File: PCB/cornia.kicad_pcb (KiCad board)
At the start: 2 copper layers, 159.3 x 104.6 mm, 76 parts, among them J1 Conn_01x01_Pin, SW1 SW_Push, SW10 SW_Push, SW11 SW_Push, SW12 SW_Push, SW13 SW_Push, SW14 SW_Push, SW15 SW_Push, SW16 SW_Push, SW17 SW_Push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

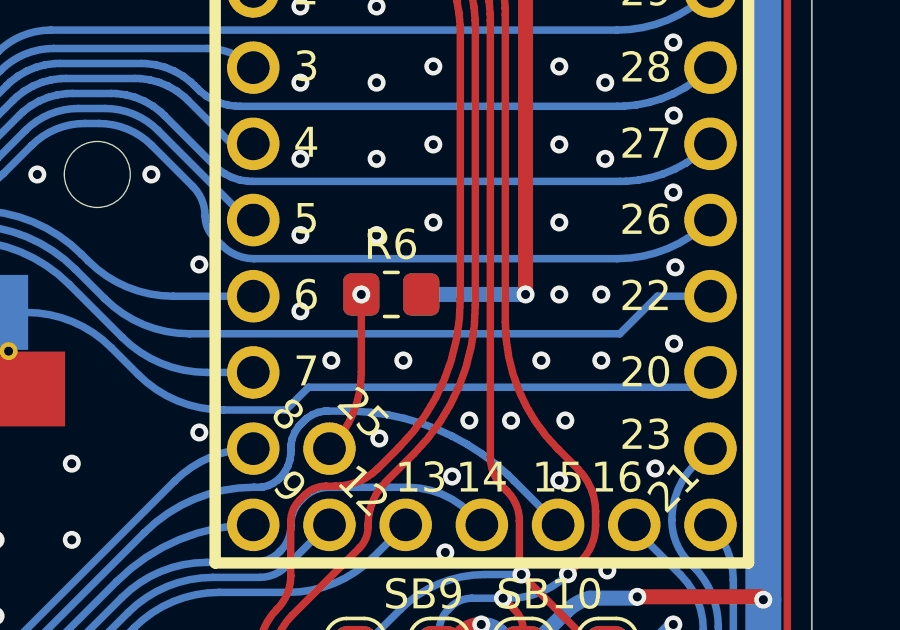
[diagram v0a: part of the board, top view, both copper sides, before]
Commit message: [PCB/Output] Add teardrop + update output
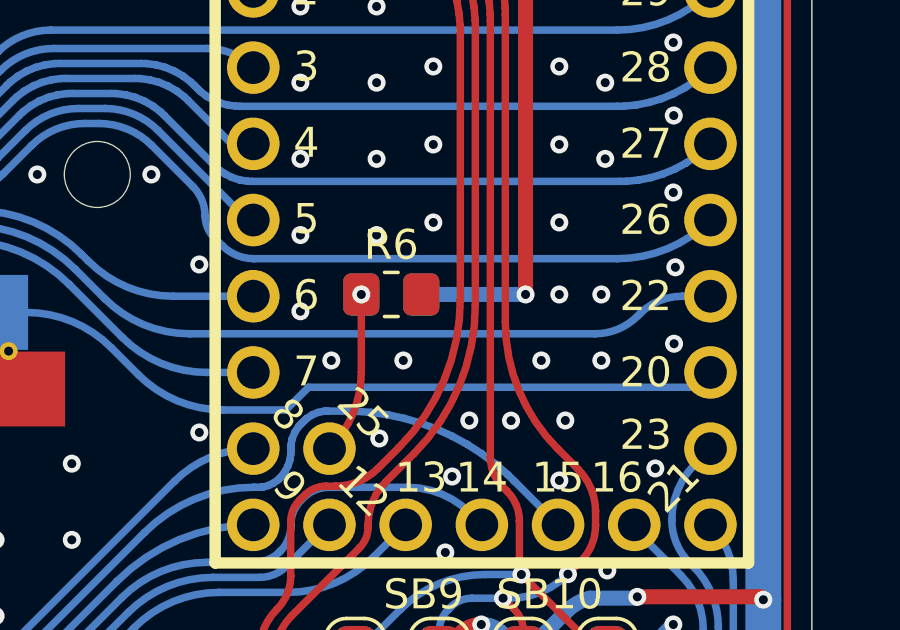
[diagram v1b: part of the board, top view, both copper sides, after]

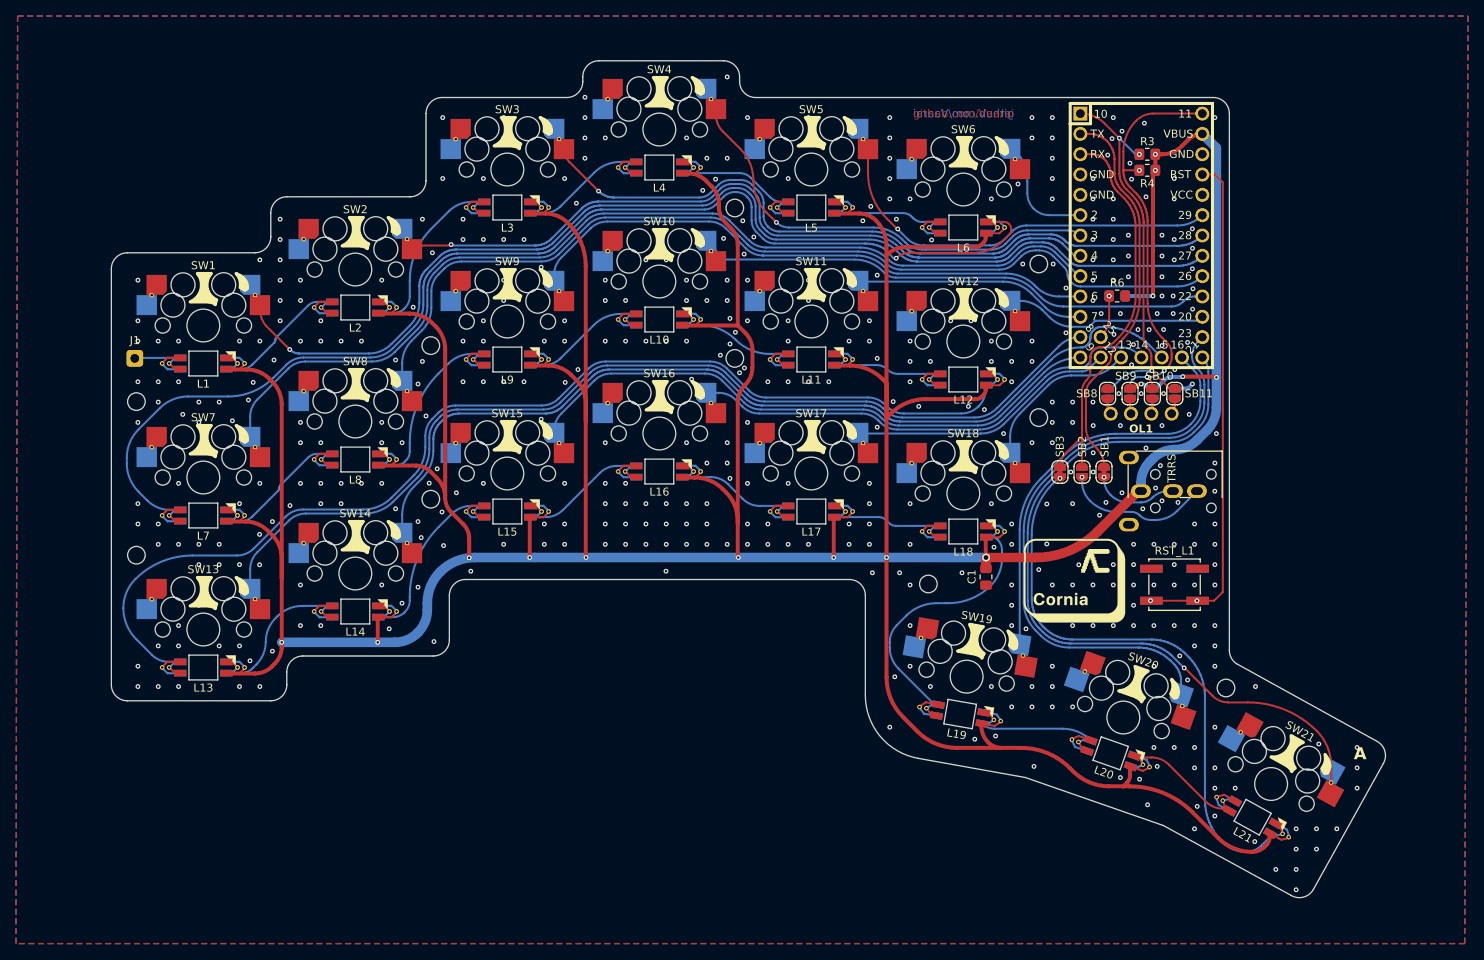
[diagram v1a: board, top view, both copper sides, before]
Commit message: [PCB] Fix RGB Led pin assignment mistake
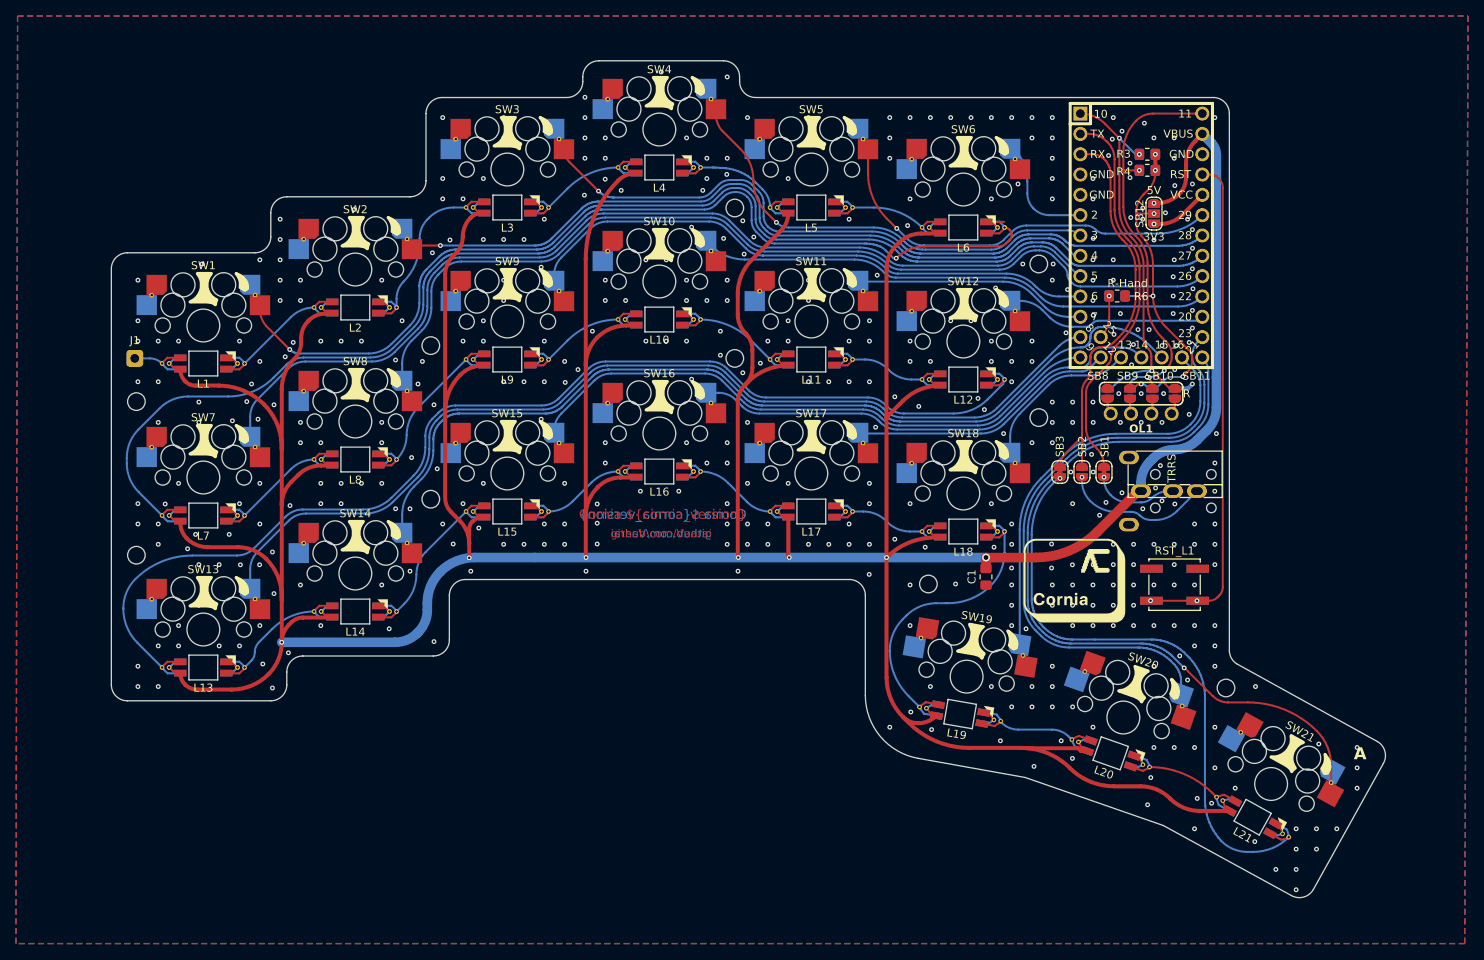
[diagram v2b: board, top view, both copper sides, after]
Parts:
- added SB12: SolderJumper_3_Open, cornia-footprints:SolderJumper-3_I2C, F.Cu at (149.0, 40.7)
- added SB13: SolderJumper_3_Open, cornia-footprints:SolderJumper-3_I2C, B.Cu at (149.0, 40.7)
- SB10, SB11, SB4, SB5, SB6, SB7, SB8, SB9: footprint cornia-footprints:SolderJumper-2_Open -> cornia-footprints:SolderJumper-2_Open_NoSilk
- U2: footprint cornia-footprints:TRRS -> cornia-footprints:TRRS_PJ-320A
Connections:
- L1 pad 1: Net-(J1-Pin_1) -> VBUS
- L1 pad 2: GND -> Net-(J1-Pin_1)
- L1 pad 3: Net-(L1-DIN) -> GND
- L1 pad 4: VBUS -> Net-(L1-DIN)
- L10 pad 1: Net-(L10-DOUT) -> VBUS
- L10 pad 2: GND -> Net-(L10-DOUT)
- L10 pad 3: Net-(L10-DIN) -> GND
- L10 pad 4: VBUS -> Net-(L10-DIN)
- L11 pad 1: Net-(L10-DIN) -> VBUS
- L11 pad 2: GND -> Net-(L10-DIN)
- L11 pad 3: Net-(L11-DIN) -> GND
- L11 pad 4: VBUS -> Net-(L11-DIN)
- L12 pad 1: Net-(L11-DIN) -> VBUS
- L12 pad 2: GND -> Net-(L11-DIN)
- L12 pad 3: Net-(L12-DIN) -> GND
- L12 pad 4: VBUS -> Net-(L12-DIN)
- L13 pad 1: Net-(L12-DIN) -> VBUS
- L13 pad 2: GND -> Net-(L12-DIN)
- L13 pad 3: Net-(L13-DIN) -> GND
- L13 pad 4: VBUS -> Net-(L13-DIN)
- L14 pad 1: Net-(L13-DIN) -> VBUS
- L14 pad 2: GND -> Net-(L13-DIN)
- L14 pad 3: Net-(L14-DIN) -> GND
- L14 pad 4: VBUS -> Net-(L14-DIN)
- L15 pad 1: Net-(L14-DIN) -> VBUS
- L15 pad 2: GND -> Net-(L14-DIN)
- L15 pad 3: Net-(L15-DIN) -> GND
- L15 pad 4: VBUS -> Net-(L15-DIN)
- L16 pad 1: Net-(L15-DIN) -> VBUS
- L16 pad 2: GND -> Net-(L15-DIN)
- L16 pad 3: Net-(L16-DIN) -> GND
- L16 pad 4: VBUS -> Net-(L16-DIN)
- L17 pad 1: Net-(L16-DIN) -> VBUS
- L17 pad 2: GND -> Net-(L16-DIN)
- L17 pad 3: Net-(L17-DIN) -> GND
- L17 pad 4: VBUS -> Net-(L17-DIN)
- L18 pad 1: Net-(L17-DIN) -> VBUS
- L18 pad 2: GND -> Net-(L17-DIN)
- L18 pad 3: Net-(L18-DIN) -> GND
- L18 pad 4: VBUS -> Net-(L18-DIN)
- L19 pad 1: Net-(L18-DIN) -> VBUS
- L19 pad 2: GND -> Net-(L18-DIN)
- L19 pad 3: Net-(L19-DIN) -> GND
- L19 pad 4: VBUS -> Net-(L19-DIN)
- L2 pad 1: Net-(L1-DIN) -> VBUS
- L2 pad 2: GND -> Net-(L1-DIN)
- L2 pad 3: Net-(L2-DIN) -> GND
- L2 pad 4: VBUS -> Net-(L2-DIN)
- L20 pad 1: Net-(L19-DIN) -> VBUS
- L20 pad 2: GND -> Net-(L19-DIN)
- L20 pad 3: Net-(L20-DIN) -> GND
- L20 pad 4: VBUS -> Net-(L20-DIN)
- L21 pad 1: Net-(L20-DIN) -> VBUS
- L21 pad 2: GND -> Net-(L20-DIN)
- L21 pad 3: /LED -> GND
- L21 pad 4: VBUS -> /LED
- L3 pad 1: Net-(L2-DIN) -> VBUS
- L3 pad 2: GND -> Net-(L2-DIN)
- L3 pad 3: Net-(L3-DIN) -> GND
- L3 pad 4: VBUS -> Net-(L3-DIN)
- L4 pad 1: Net-(L3-DIN) -> VBUS
- L4 pad 2: GND -> Net-(L3-DIN)
- L4 pad 3: Net-(L4-DIN) -> GND
- L4 pad 4: VBUS -> Net-(L4-DIN)
- L5 pad 1: Net-(L4-DIN) -> VBUS
- L5 pad 2: GND -> Net-(L4-DIN)
- L5 pad 3: Net-(L5-DIN) -> GND
- L5 pad 4: VBUS -> Net-(L5-DIN)
- L6 pad 1: Net-(L5-DIN) -> VBUS
- L6 pad 2: GND -> Net-(L5-DIN)
- L6 pad 3: Net-(L6-DIN) -> GND
- L6 pad 4: VBUS -> Net-(L6-DIN)
- L7 pad 1: Net-(L6-DIN) -> VBUS
- L7 pad 2: GND -> Net-(L6-DIN)
- L7 pad 3: Net-(L7-DIN) -> GND
- L7 pad 4: VBUS -> Net-(L7-DIN)
- L8 pad 1: Net-(L7-DIN) -> VBUS
- L8 pad 2: GND -> Net-(L7-DIN)
- L8 pad 3: Net-(L8-DIN) -> GND
- L8 pad 4: VBUS -> Net-(L8-DIN)
- L9 pad 1: Net-(L8-DIN) -> VBUS
- L9 pad 2: GND -> Net-(L8-DIN)
- L9 pad 3: Net-(L10-DOUT) -> GND
- L9 pad 4: VBUS -> Net-(L10-DOUT)
- R1 pad 1: VBUS -> VI2C
- R2 pad 1: VBUS -> VI2C
- R3 pad 1: VBUS -> VI2C
- R4 pad 1: VBUS -> VI2C
- R5 pad 1: VBUS -> VI2C
- SB6 pad 1: VBUS -> VI2C
- SB9 pad 1: VBUS -> VI2C
- U1 pad 27: unconnected-(U1-VCC-Pad27) -> VCC
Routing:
- net VI2C: track 0.00 -> 44.8 mm, vias 0 -> 6
- net VBUS: track 629.6 -> 619.4 mm, vias 15 -> 8
- net VCC: track 0.00 -> 7.35 mm, vias 0 -> 1
- net Net-(L8-DIN): track 22.2 -> 15.7 mm
- net Net-(L14-DIN): track 22.0 -> 15.7 mm
- net Net-(L13-DIN): track 18.2 -> 11.9 mm
- net Net-(L20-DIN): track 15.0 -> 9.41 mm
- net Net-(L7-DIN): track 16.9 -> 11.4 mm
- net Net-(L1-DIN): track 16.9 -> 11.4 mm
- net Net-(L15-DIN): track 15.8 -> 10.3 mm
- net Net-(L3-DIN): track 15.7 -> 10.3 mm
- net Net-(L10-DOUT): track 15.7 -> 10.3 mm
- net Net-(L6-DIN): track 147.6 -> 142.5 mm
- net Net-(L2-DIN): track 22.2 -> 17.2 mm
- net Net-(L19-DIN): track 14.3 -> 9.62 mm
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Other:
- board text added: "Cornia ${cornia_version}"
- board text added: "L"
- board text added: "L-Hand"
- board text added: "R"
- board text added: "R-Hand"

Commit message: [PCB] Multiple fix based on v1RC2 board bring-up
- Reduce RST thermal relief width
- Update SB silkscreen
- Update TRRS silkscreen
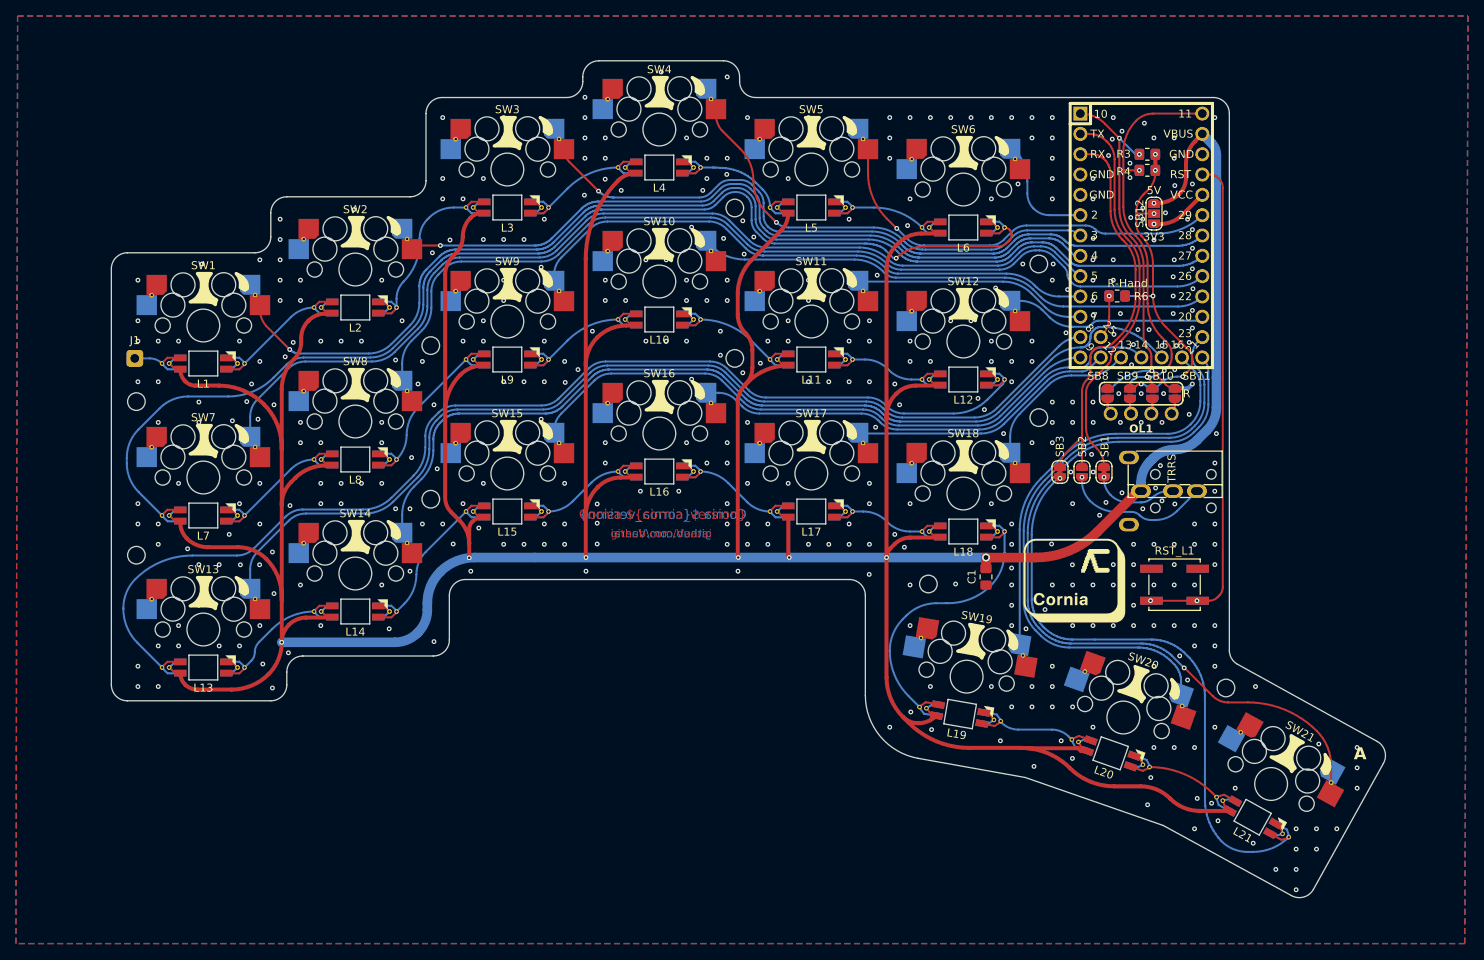
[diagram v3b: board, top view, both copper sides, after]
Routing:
- net GND: track 4.92 -> 2.43 mm, vias 452 -> 445
- net VBUS: track 619.4 -> 620.1 mm

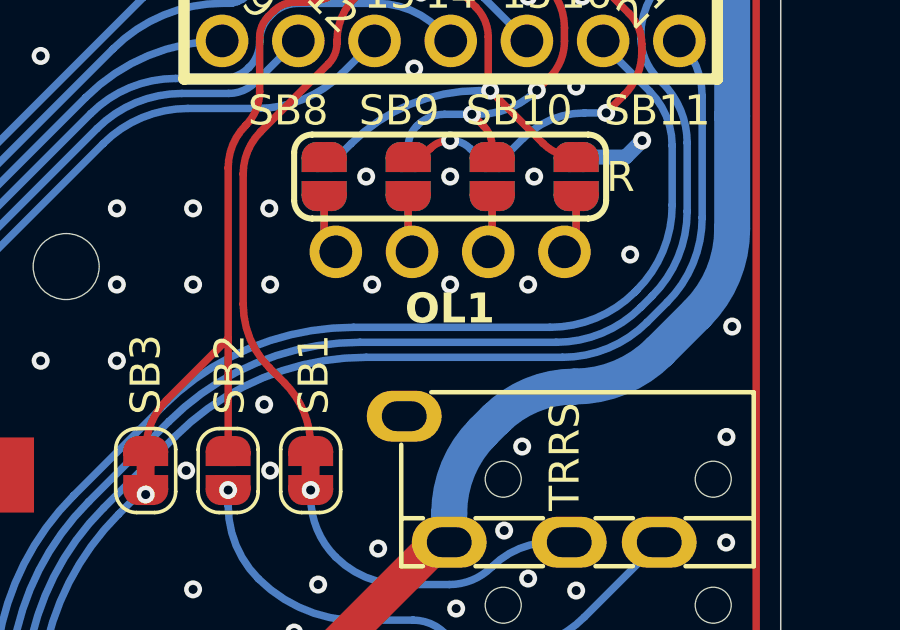
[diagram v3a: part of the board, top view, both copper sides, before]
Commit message: [PCB DRC] Enable 'hole to hole' DRC and fix all issues
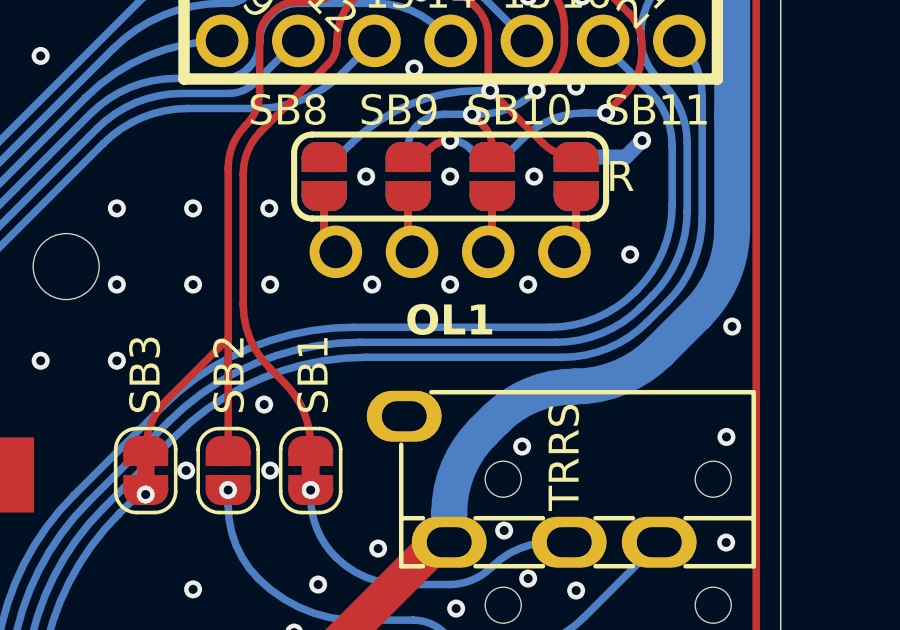
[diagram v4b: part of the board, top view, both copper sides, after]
